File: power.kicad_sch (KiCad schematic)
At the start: 8 parts

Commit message: Add title block
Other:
- company: (none) -> Matteo Golin
- title: (none) -> Pygmy
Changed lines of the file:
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@@
 	(generator_version "8.0")
 	(paper "A4")
+	(title_block
+		(title "Pygmy")
+		(date "2024-11-13")
+		(rev "A")
+		(company "Matteo Golin")
+	)
 	(junction
 		(at 180.34 73.66)

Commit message: Added decoupling caps to RN2483 and fixed antenna connection. Also settled on easy GPS.
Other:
- moved on the sheet: J?
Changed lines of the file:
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@@
+	)
+	(junction
+		(at 184.15 73.66)
+		(diameter 0)
+		(color 0 0 0 0)
 	)
 	(junction
@@
 	(wire
 		(pts
+			(xy 180.34 73.66) (xy 184.15 73.66)
+		)
+		(stroke
+			(width 0)
+			(type default)
+		)
+	)
+	(wire
+		(pts
 			(xy 76.2 132.08) (xy 76.2 134.62)
 		)
@@
 	(wire
 		(pts
+			(xy 184.15 72.39) (xy 184.15 73.66)
+		)
+		(stroke
+			(width 0)
+			(type default)
+		)
+	)
+	(wire
+		(pts
 			(xy 78.74 77.47) (xy 78.74 80.01)
 		)
@@
 	(wire
 		(pts
-			(xy 186.69 62.23) (xy 186.69 63.5)
+			(xy 191.77 62.23) (xy 191.77 63.5)
 		)
 		(stroke
@@
 	(wire
 		(pts
-			(xy 186.69 62.23) (xy 190.5 62.23)
+			(xy 191.77 62.23) (xy 195.58 62.23)
 		)
 		(stroke
@@
 	(wire
 		(pts
+			(xy 184.15 73.66) (xy 195.58 73.66)
+		)
+		(stroke
+			(width 0)
+			(type default)
+		)
+	)
+	(wire
+		(pts
 			(xy 121.92 82.55) (xy 121.92 77.47)
 		)
@@
 	(wire
 		(pts
-			(xy 180.34 73.66) (xy 190.5 73.66)
-		)
-		(stroke
-			(width 0)
-			(type default)
-		)
-	)
-	(wire
-		(pts
 			(xy 88.9 87.63) (xy 88.9 90.17)
 		)
@@
 	(wire
 		(pts
-			(xy 190.5 62.23) (xy 190.5 71.12)
+			(xy 195.58 62.23) (xy 195.58 71.12)
 		)
 		(stroke
@@
 	)
 	(symbol
+		(lib_id "power:PWR_FLAG")
+		(at 184.15 72.39 0)
+		(unit 1)
+		(exclude_from_sim no)
+		(in_bom yes)
+		(on_board yes)
+		(dnp no)
+		(fields_autoplaced yes)
+		(property "Reference" "#FLG01"
+			(at 184.15 70.485 0)
+			(effects
+				(font
+					(size 1.27 1.27)
+				)
+				(hide yes)
+			)
+		)
+		(property "Value" "~"
+			(at 184.15 68.58 0)
+			(effects
+				(font
+					(size 1.27 1.27)
+				)
+			)
+		)
+		(property "Footprint" ""
+			(at 184.15 72.39 0)
+			(effects
+				(font
+					(size 1.27 1.27)
+				)
+				(hide yes)
+			)
+		)
+		(property "Datasheet" "~"
+			(at 184.15 72.39 0)
+			(effects
+				(font
+					(size 1.27 1.27)
+				)
+				(hide yes)
+			)
+		)
+		(property "Description" "Special symbol for telling ERC where power comes from"
+			(at 184.15 72.39 0)
+			(effects
+				(font
+					(size 1.27 1.27)
+				)
+				(hide yes)
+			)
+		)
+		(pin "1"
+		)
+		(instances
+			(project ""
+				(path "/b90d3133-97a4-4747-8a68-e80f353c7b97/8d42d8f3-e666-4352-a3e9-99ac4271efe0"
+					(reference "#FLG01")
+					(unit 1)
+				)
+			)
+		)
+	)
+	(symbol
 		(lib_id "Device:R")
 		(at 134.62 140.97 0)
@@
 	(symbol
 		(lib_id "Connector_Generic:Conn_01x02")
-		(at 195.58 71.12 0)
+		(at 200.66 71.12 0)
 		(unit 1)
 		(exclude_from_sim no)
@@
 		(fields_autoplaced yes)
 		(property "Reference" "J?"
-			(at 198.12 71.1199 0)
+			(at 203.2 71.1199 0)
 			(effects
 				(font
@@
 		)
 		(property "Value" "Conn_01x02"
-			(at 198.12 73.6599 0)
+			(at 203.2 73.6599 0)
 			(effects
 				(font
@@
 		)
 		(property "Footprint" "Connector_JST:JST_PH_S2B-PH-K_1x02_P2.00mm_Horizontal"
-			(at 195.58 71.12 0)
+			(at 200.66 71.12 0)
 			(effects
 				(font
@@
 		)
 		(property "Datasheet" "~"
-			(at 195.58 71.12 0)
+			(at 200.66 71.12 0)
 			(effects
 				(font
@@
 		)
 		(property "Description" "Generic connector, single row, 01x02, script generated (kicad-library-utils/schlib/autogen/connector/)"
-			(at 195.58 71.12 0)
+			(at 200.66 71.12 0)
 			(effects
 				(font
@@
 	(symbol
 		(lib_id "power:GND")
-		(at 186.69 63.5 0)
+		(at 191.77 63.5 0)
 		(unit 1)
 		(exclude_from_sim no)
@@
 		(fields_autoplaced yes)
 		(property "Reference" "#PWR061"
-			(at 186.69 69.85 0)
+			(at 191.77 69.85 0)
 			(effects
 				(font
@@
 		)
 		(property "Value" "GND"
-			(at 186.69 68.58 0)
+			(at 191.77 68.58 0)
 			(effects
 				(font
@@
 		)
 		(property "Footprint" ""
-			(at 186.69 63.5 0)
+			(at 191.77 63.5 0)
 			(effects
 				(font
@@
 		)
 		(property "Datasheet" ""
-			(at 186.69 63.5 0)
+			(at 191.77 63.5 0)
 			(effects
 				(font
@@
 		)
 		(property "Description" "Power symbol creates a global label with name \"GND\" , ground"
-			(at 186.69 63.5 0)
-			(effects
-				(font
+			(at 191.77 63.5 0)
+			(effects
+				(font

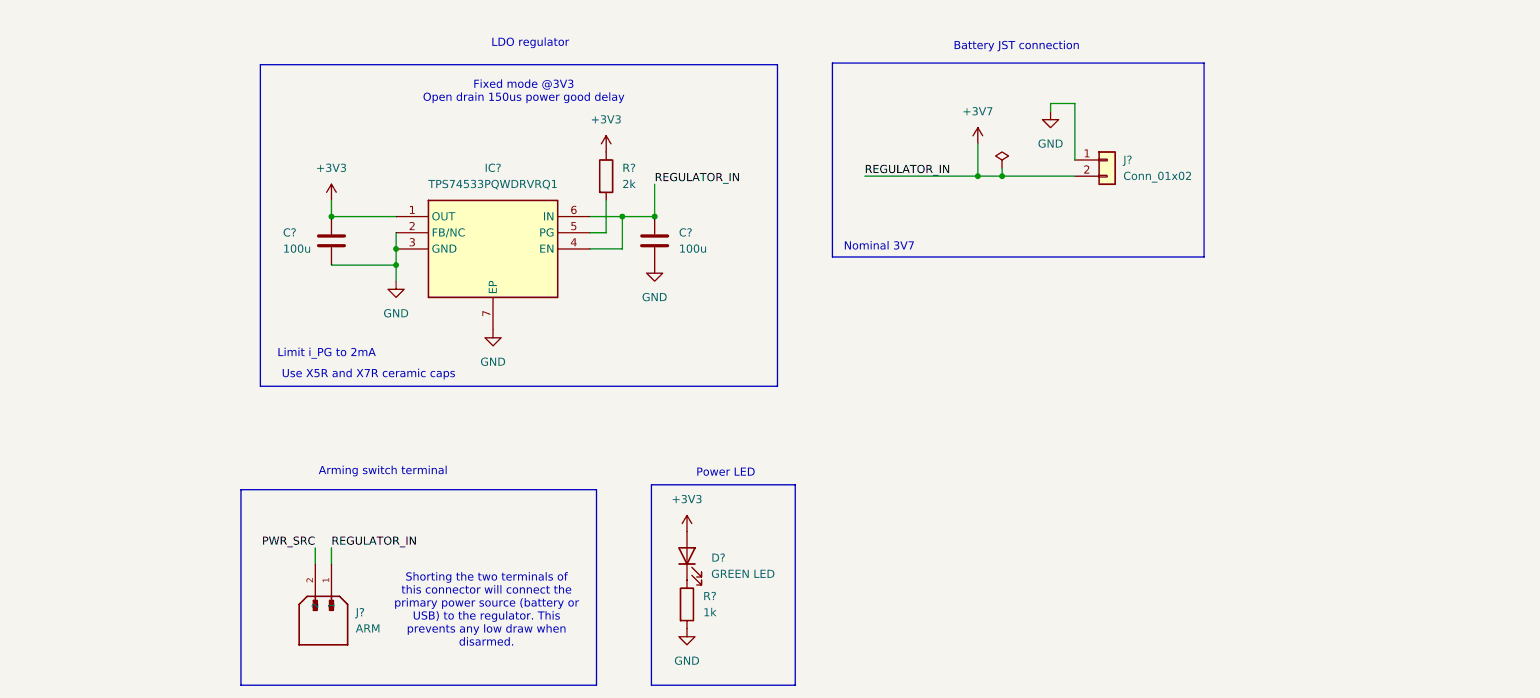
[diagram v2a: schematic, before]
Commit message: Updated power supply to use buck regulator and power input MUX. Also computed current draw of the board to size power regulator.
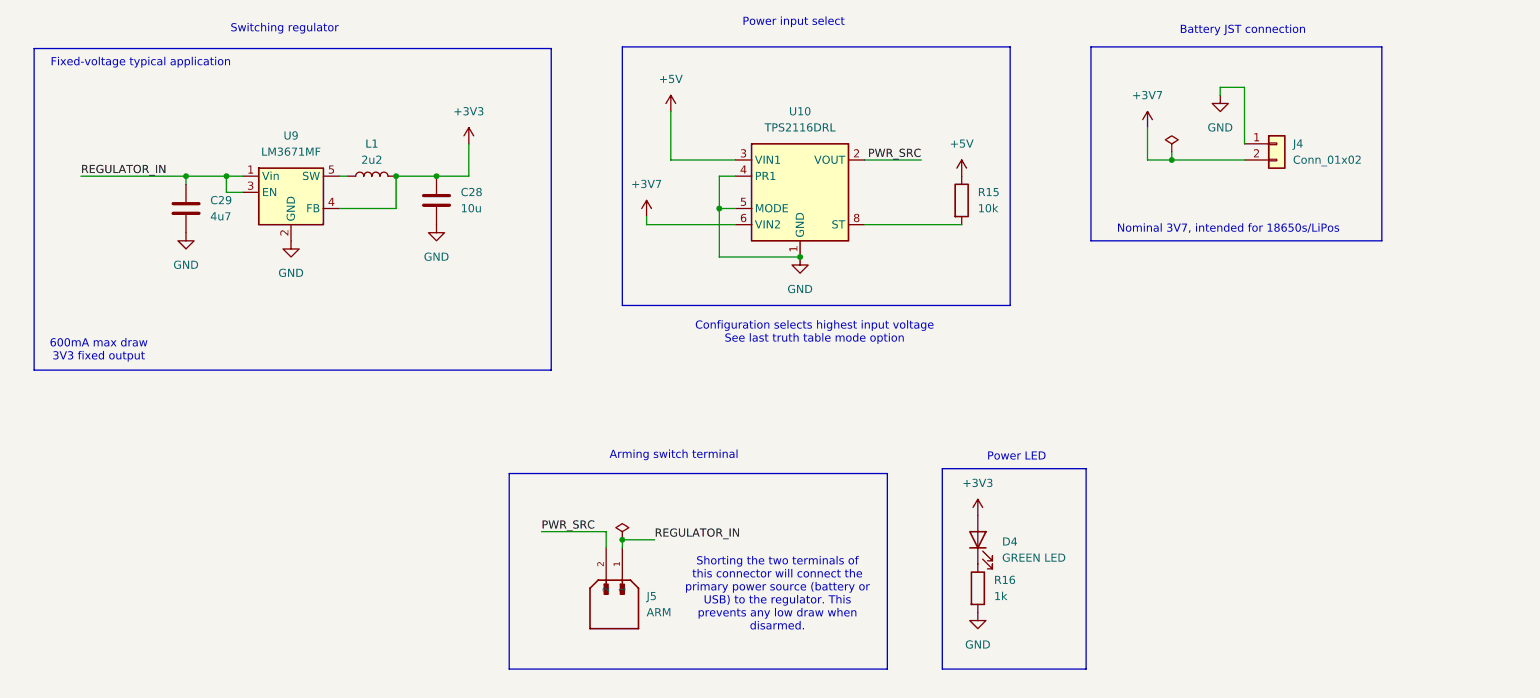
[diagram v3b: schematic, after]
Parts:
- removed C? (x2): 100u, symbol Device:C
- removed IC?: TPS74533PQWDRVRQ1, regulator:SON65P200X200X80-7N, symbol TPS74533PQWDRVRQ1:TPS74533PQWDRVRQ1
- removed R?: 2k, symbol Device:R
- added C28: 10u, symbol Device:C
- added C29: 4u7, symbol Device:C
- added L1: 2u2, symbol Device:L
- added R15: 10k, symbol Device:R
- added U10: TPS2116DRL, Package_TO_SOT_SMD:SOT-583-8, symbol Power_Management:TPS2116DRL
- added U9: LM3671MF, Package_TO_SOT_SMD:TSOT-23-5, symbol Regulator_Switching:LM3670MF
- gave numbers to parts that had none: 4
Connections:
- net +3V3: now also C28.1, L1.2, U9.4 (FB)
- net +3V7: now also U10.6 (VIN2); no longer J5.1
- net GND: now also C28.2, C29.2, U10.1 (GND), U10.4 (PR1), U10.5 (MODE), U9.2 (GND)
- net PWR_SRC: now also U10.2 (VOUT), U10.7 (VOUT)
- new net: R15.2, U10.8 (ST)
- new net: L1.1, U9.5 (SW)
- new net +5V: R15.1, U10.3 (VIN1)
- new net REGULATOR_IN: C29.1, J5.1, U9.1 (Vin), U9.3 (EN)
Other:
- note added: "600mA max draw 3V3 fixed output"
- note added: "Configuration selects highest input voltage See last truth table mode option"
- note added: "Fixed-voltage typical application"
- note added: "Nominal 3V7, intended for 18650s/LiPos"
- note added: "Power input select"
- note added: "Switching regulator"
- note removed: "Fixed mode @3V3 Open drain 150us power good delay"
- note removed: "LDO regulator"
- note removed: "Limit i_PG to 2mA"
- note removed: "Nominal 3V7"
- note removed: "Use X5R and X7R ceramic caps"
- moved on the sheet: D4, J4, J5, R16

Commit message: Added capacitors to MUX to supply transient power when switching.
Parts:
- added C28, C29, C32: 1u, symbol Device:C
- renumbered C28 to C30, C29 to C31
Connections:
- net +3V7: now also C32.1
- net +5V: now also C29.1
- net GND: now also C28.2, C29.2, C32.2
- net PWR_SRC: now also C28.1
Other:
- moved on the sheet: J4, R15, U10

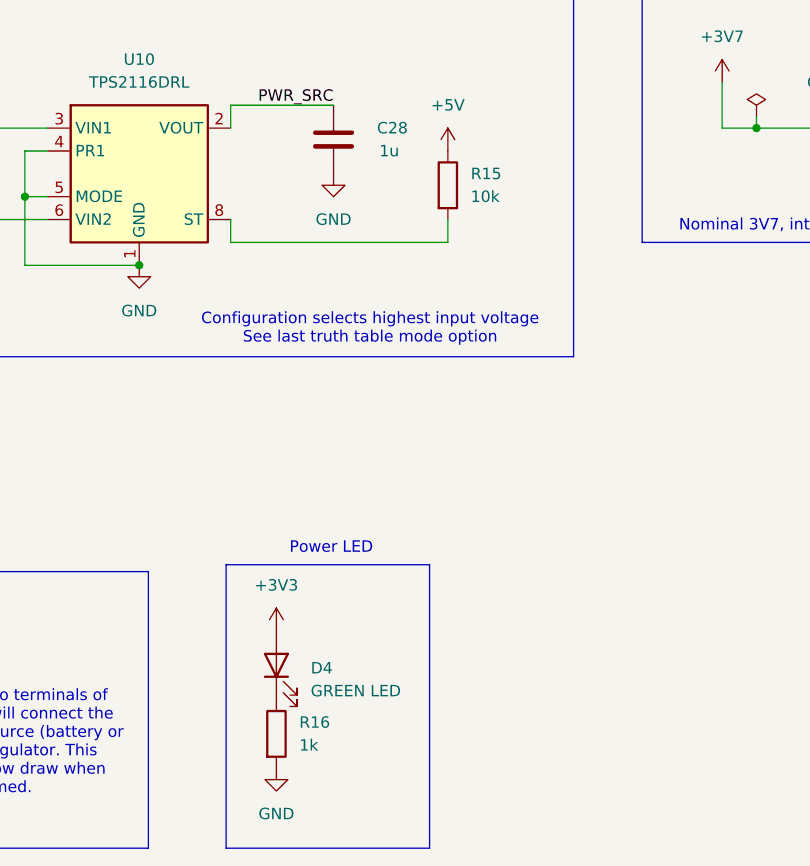
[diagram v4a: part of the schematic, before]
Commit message: Added footprints for all components
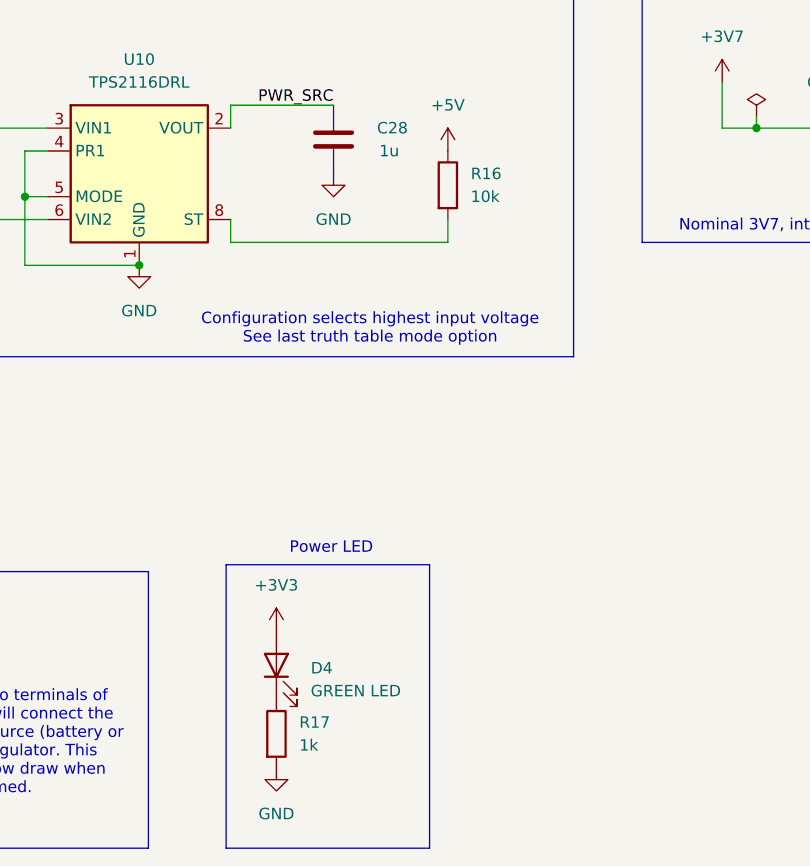
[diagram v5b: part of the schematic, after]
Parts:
- C28, C29, C31, C32: footprint (none) -> Capacitor_SMD:C_0603_1608Metric
- C30: footprint (none) -> Capacitor_SMD:C_0805_2012Metric
- D4: footprint (none) -> LED_SMD:LED_0805_2012Metric
- J5: footprint minifit-jr:MOLEX_1726480102 -> TerminalBlock_Phoenix:TerminalBlock_Phoenix_MKDS-1,5-2_1x02_P5.00mm_Horizontal
- L1: footprint (none) -> Inductor_SMD:L_0805_2012Metric
- R16: renamed from R15; footprint (none) -> Resistor_SMD:R_0201_0603Metric
- R17: renamed from R16; footprint (none) -> Resistor_SMD:R_0201_0603Metric
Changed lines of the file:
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@@
 			)
 		)
-		(property "Footprint" "minifit-jr:MOLEX_1726480102"
+		(property "Footprint" "TerminalBlock_Phoenix:TerminalBlock_Phoenix_MKDS-1,5-2_1x02_P5.00mm_Horizontal"
 			(at 124.46 137.16 0)
 			(effects
@@
 		(dnp no)
 		(fields_autoplaced yes)
-		(property "Reference" "R15"
+		(property "Reference" "R16"
 			(at 201.93 76.1999 0)
 			(effects
@@
 			)
 		)
-		(property "Footprint" ""
+		(property "Footprint" "Resistor_SMD:R_0201_0603Metric"
 			(at 197.612 77.47 90)
 			(effects
@@
 			(project ""
 				(path "/b90d3133-97a4-4747-8a68-e80f353c7b97/8d42d8f3-e666-4352-a3e9-99ac4271efe0"
-					(reference "R15")
+					(reference "R16")
 					(unit 1)
 				)
@@
 			)
 		)
-		(property "Footprint" ""
+		(property "Footprint" "Capacitor_SMD:C_0603_1608Metric"
 			(at 56.8452 82.55 0)
 			(effects
@@
 		(dnp no)
 		(fields_autoplaced yes)
-		(property "Reference" "R16"
+		(property "Reference" "R17"
 			(at 182.88 137.1599 0)
 			(effects
@@
 			)
 		)
-		(property "Footprint" ""
+		(property "Footprint" "Resistor_SMD:R_0201_0603Metric"
 			(at 178.562 138.43 90)
 			(effects
@@
 			(project "flight-computer"
 				(path "/b90d3133-97a4-4747-8a68-e80f353c7b97/8d42d8f3-e666-4352-a3e9-99ac4271efe0"
-					(reference "R16")
+					(reference "R17")
 					(unit 1)
 				)
@@
 			)
 		)
-		(property "Footprint" ""
+		(property "Footprint" "Inductor_SMD:L_0805_2012Metric"
 			(at 85.09 73.66 0)
 			(effects
@@
 			)
 		)
-		(property "Footprint" ""
+		(property "Footprint" "LED_SMD:LED_0805_2012Metric"
 			(at 180.34 130.81 0)
 			(effects
@@
 			)
 		)
-		(property "Footprint" ""
+		(property "Footprint" "Capacitor_SMD:C_0603_1608Metric"
 			(at 143.2052 78.74 0)
 			(effects
@@
 			)
 		)
-		(property "Footprint" ""
+		(property "Footprint" "Capacitor_SMD:C_0603_1608Metric"
 			(at 134.3152 88.9 0)
 			(effects
@@
 			)
 		)
-		(property "Footprint" ""
+		(property "Footprint" "Capacitor_SMD:C_0603_1608Metric"
 			(at 187.6552 76.2 0)
 			(effects
@@
 			)
 		)
-		(property "Footprint" ""
+		(property "Footprint" "Capacitor_SMD:C_0805_2012Metric"
 			(at 96.2152 81.28 0)
 			(effects
